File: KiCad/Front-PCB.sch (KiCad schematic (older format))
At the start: 0 parts

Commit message: front PCB schematic complete
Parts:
- added J1: CONN_01X20, symbol CONN_01X20
- added R19: R, symbol R
- added S1-Left, S2-Up, S3-Right, S4-Down: RP3502, symbol RP3502
- added S5-Start, S6-Stop: RP3508, symbol RP3508
- added S7-Door-Contact: A0151B, symbol A0151B
- added U?: MAX7219, symbol MAX7219
- added U?: LTC-4727JR, symbol LTC-4727JR
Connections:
- net labels added: +5V, GND
- wire segments 0 -> 96
- no-connect marks 0 -> 4

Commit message: front panel erc
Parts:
- removed U?: MAX7219, symbol MAX7219
- removed U?: LTC-4727JR, symbol LTC-4727JR
- added R1, R2, R3, R4, R5, R6: 1k, symbol R
- added R20, R21: 500, symbol R
- added U1: MAX7219, symbol MAX7219
- added U2: LTC-4727JR, symbol LTC-4727JR
- J1: value CONN_01X20 -> HLW20R-2C7LF
- R19: value R -> 10k
- S1: renamed from S1-Left; symbol RP3502 -> RP3502-RESCUE-Front-PCB
- S2: renamed from S2-Up; symbol RP3502 -> RP3502-RESCUE-Front-PCB
- S3: renamed from S3-Right; symbol RP3502 -> RP3502-RESCUE-Front-PCB
- S4: renamed from S4-Down; symbol RP3502 -> RP3502-RESCUE-Front-PCB
- S5: renamed from S5-Start; symbol RP3508 -> RP3508-RESCUE-Front-PCB
- S6: renamed from S6-Stop; symbol RP3508 -> RP3508-RESCUE-Front-PCB
- renumbered S7-Door-Contact to S7
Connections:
- wire segments 96 -> 109
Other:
- moved on the sheet: S3

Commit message: kicad footprints and unrouted layout
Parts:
- added P1: Mounting Vias, Easy-PCB-footprints:10-32, symbol CONN_01X01
- added P2, P3, P4: CONN_01X01, Easy-PCB-footprints:10-32, symbol CONN_01X01
- J1: footprint (none) -> Easy-PCB-Footprints:HLW20R-2C7LF
- R1, R19, R2, R20, R21, R3, R4, R5, R6: footprint (none) -> Discret:R4
- S1, S2, S3, S4: footprint (none) -> Easy-PCB-Footprints:RP3502
- S5, S6: footprint (none) -> Easy-PCB-Footprints:RP3508; symbol RP3508-RESCUE-Front-PCB -> RP3508
- S7: footprint (none) -> Easy-PCB-Footprints:A0151B
- U1: footprint (none) -> Easy-PCB-footprints:4824-3000-CP
- U2: footprint (none) -> Easy-PCB-footprints:LTC-4727JR
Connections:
- wire segments 109 -> 115
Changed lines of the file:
@@
 F 0 "R19" V 9230 1800 50  0000 C CNN
 F 1 "10k" V 9150 1800 50  0000 C CNN
-F 2 "" V 9080 1800 30  0000 C CNN
+F 2 "Discret:R4" V 9080 1800 30  0001 C CNN
 F 3 "" H 9150 1800 30  0000 C CNN
 	1    9150 1800
@@
 F 0 "S1" H 1300 6400 60  0000 C CNN
 F 1 "RP3502" H 1300 5900 60  0000 C CNN
-F 2 "" H 1300 6050 60  0000 C CNN
+F 2 "Easy-PCB-Footprints:RP3502" H 1300 6050 60  0001 C CNN
 F 3 "" H 1300 6050 60  0000 C CNN
 	1    1300 6050
@@
 F 0 "S4" H 2300 6800 60  0000 C CNN
 F 1 "RP3502" H 2300 6300 60  0000 C CNN
-F 2 "" H 2300 6450 60  0000 C CNN
+F 2 "Easy-PCB-Footprints:RP3502" H 2300 6450 60  0001 C CNN
 F 3 "" H 2300 6450 60  0000 C CNN
 	1    2300 6450
@@
 F 0 "S2" H 2400 6050 60  0000 C CNN
 F 1 "RP3502" H 2400 5550 60  0000 C CNN
-F 2 "" H 2400 5700 60  0000 C CNN
+F 2 "Easy-PCB-Footprints:RP3502" H 2400 5700 60  0001 C CNN
 F 3 "" H 2400 5700 60  0000 C CNN
 	1    2400 5700
@@
 F 0 "S3" H 3500 6350 60  0000 C CNN
 F 1 "RP3502" H 3500 5850 60  0000 C CNN
-F 2 "" H 3500 6000 60  0000 C CNN
+F 2 "Easy-PCB-Footprints:RP3502" H 3500 6000 60  0001 C CNN
 F 3 "" H 3500 6000 60  0000 C CNN
 	1    3500 6000
@@
 $EndComp
 $Comp
-L RP3508-RESCUE-Front-PCB S5
+L RP3508 S5
 U 1 1 5652B631
 P 4500 6000
 F 0 "S5" H 4500 6500 60  0000 C CNN
 F 1 "RP3508" H 4500 6400 60  0000 C CNN
-F 2 "" H 4500 6000 60  0000 C CNN
+F 2 "Easy-PCB-Footprints:RP3508" H 4500 6000 60  0001 C CNN
 F 3 "" H 4500 6000 60  0000 C CNN
 	1    4500 6000
@@
 $EndComp
 $Comp
-L RP3508-RESCUE-Front-PCB S6
+L RP3508 S6
 U 1 1 5652B70B
 P 5800 6200
 F 0 "S6" H 5800 6700 60  0000 C CNN
 F 1 "RP3508" H 5800 6600 60  0000 C CNN
-F 2 "" H 5800 6200 60  0000 C CNN
+F 2 "Easy-PCB-Footprints:RP3508" H 5800 6200 60  0001 C CNN
 F 3 "" H 5800 6200 60  0000 C CNN
 	1    5800 6200
@@
 F 0 "S7" H 3900 7850 60  0000 C CNN
 F 1 "A0151B" H 3900 6800 60  0000 C CNN
-F 2 "" H 3900 7250 60  0000 C CNN
+F 2 "Easy-PCB-Footprints:A0151B" H 3900 7250 60  0001 C CNN
 F 3 "" H 3900 7250 60  0000 C CNN
 	1    3900 7250
@@
 F 0 "R1" V 1780 6350 50  0000 C CNN
 F 1 "1k" V 1700 6350 50  0000 C CNN
-F 2 "" V 1630 6350 30  0000 C CNN
+F 2 "Discret:R4" V 1630 6350 30  0001 C CNN
 F 3 "" H 1700 6350 30  0000 C CNN
 	1    1700 6350
@@
 F 0 "R2" V 2880 5950 50  0000 C CNN
 F 1 "1k" V 2800 5950 50  0000 C CNN
-F 2 "" V 2730 5950 30  0000 C CNN
+F 2 "Discret:R4" V 2730 5950 30  0001 C CNN
 F 3 "" H 2800 5950 30  0000 C CNN
 	1    2800 5950
@@
 F 0 "R4" V 2880 6700 50  0000 C CNN
 F 1 "1k" V 2800 6700 50  0000 C CNN
-F 2 "" V 2730 6700 30  0000 C CNN
+F 2 "Discret:R4" V 2730 6700 30  0001 C CNN
 F 3 "" H 2800 6700 30  0000 C CNN
 	1    2800 6700
@@
 F 0 "R3" V 4130 6150 50  0000 C CNN
 F 1 "1k" V 4050 6150 50  0000 C CNN
-F 2 "" V 3980 6150 30  0000 C CNN
+F 2 "Discret:R4" V 3980 6150 30  0001 C CNN
 F 3 "" H 4050 6150 30  0000 C CNN
 	1    4050 6150
@@
 F 0 "R5" V 5080 6150 50  0000 C CNN
 F 1 "1k" V 5000 6150 50  0000 C CNN
-F 2 "" V 4930 6150 30  0000 C CNN
+F 2 "Discret:R4" V 4930 6150 30  0001 C CNN
 F 3 "" H 5000 6150 30  0000 C CNN
 	1    5000 6150
@@
 F 0 "R20" V 5280 6050 50  0000 C CNN
 F 1 "500" V 5200 6050 50  0000 C CNN
-F 2 "" V 5130 6050 30  0000 C CNN
+F 2 "Discret:R4" V 5130 6050 30  0001 C CNN
 F 3 "" H 5200 6050 30  0000 C CNN
 	1    5200 6050
@@
 F 0 "R6" V 6480 6200 50  0000 C CNN
 F 1 "1k" V 6400 6200 50  0000 C CNN
-F 2 "" V 6330 6200 30  0000 C CNN
+F 2 "Discret:R4" V 6330 6200 30  0001 C CNN
 F 3 "" H 6400 6200 30  0000 C CNN
 	1    6400 6200
@@
 F 0 "R21" V 6780 6000 50  0000 C CNN
 F 1 "500" V 6700 6000 50  0000 C CNN
-F 2 "" V 6630 6000 30  0000 C CNN
+F 2 "Discret:R4" V 6630 6000 30  0001 C CNN
 F 3 "" H 6700 6000 30  0000 C CNN
 	1    6700 6000
@@
 F 0 "J1" H 9900 6250 50  0000 C CNN
 F 1 "HLW20R-2C7LF" V 10050 5150 50  0000 C CNN
-F 2 "" H 9900 5150 60  0000 C CNN
+F 2 "Easy-PCB-Footprints:HLW20R-2C7LF" H 9900 5150 60  0001 C CNN
 F 3 "" H 9900 5150 60  0000 C CNN
 	1    9900 5150
@@
 F 0 "U2" H 4000 550 100 0000 L CNN
 F 1 "LTC-4727JR" H 3050 550 100 0000 C CNN
-F 2 "" H 3600 1850 60  0000 C CNN
+F 2 "Easy-PCB-footprints:LTC-4727JR" H 3600 1850 60  0001 C CNN
 F 3 "" H 3600 1850 60  0000 C CNN
 	1    3600 1850
@@
 F 0 "U1" H 8250 3350 60  0000 L CNN
 F 1 "MAX7219" H 8450 3450 60  0000 C CNN
-F 2 "" H 8300 2950 60  0000 C CNN
+F 2 "Easy-PCB-footprints:4824-3000-CP" H 8300 2950 60  0001 C CNN
 F 3 "" H 8300 2950 60  0000 C CNN
 	1    8300 2950
 	1    0    0    -1
 $EndComp
+$Comp
+L CONN_01X01 P1
+U 1 1 5655FFD6
+P 900 7000
+F 0 "P1" H 900 7100 50  0000 C CNN
+F 1 "Mounting Vias" V 1100 6650 50  0000 C CNN
+F 2 "Easy-PCB-footprints:10-32" H 900 7000 60  0001 C CNN
+F 3 "" H 900 7000 60  0000 C CNN
+	1    900  7000
+	-1   0    0    -1
+$EndComp
+$Comp
+L CONN_01X01 P2
+U 1 1 565600BD
+P 900 7250
+F 0 "P2" H 900 7350 50  0000 C CNN
+F 1 "CONN_01X01" V 1000 7250 50  0001 C CNN
+F 2 "Easy-PCB-footprints:10-32" H 900 7250 60  0001 C CNN
+F 3 "" H 900 7250 60  0000 C CNN
+	1    900  7250
+	-1   0    0    -1
+$EndComp
+$Comp
+L CONN_01X01 P3
+U 1 1 5656018C
+P 900 7500
+F 0 "P3" H 900 7600 50  0000 C CNN
+F 1 "CONN_01X01" V 1000 7500 50  0001 C CNN
+F 2 "Easy-PCB-footprints:10-32" H 900 7500 60  0001 C CNN
+F 3 "" H 900 7500 60  0000 C CNN
+	1    900  7500
+	-1   0    0    -1
+$EndComp
+$Comp
+L CONN_01X01 P4
+U 1 1 565601F5
+P 900 7750
+F 0 "P4" H 900 7850 50  0000 C CNN
+F 1 "CONN_01X01" V 1000 7750 50  0001 C CNN
+F 2 "Easy-PCB-footprints:10-32" H 900 7750 60  0001 C CNN
+F 3 "" H 900 7750 60  0000 C CNN
+	1    900  7750
+	-1   0    0    -1
+$EndComp
+$Comp
+L GND #PWR015
+U 1 1 56560FC4
+P 1400 7350
+F 0 "#PWR015" H 1400 7100 50  0001 C CNN
+F 1 "GND" H 1400 7200 50  0000 C CNN
+F 2 "" H 1400 7350 60  0000 C CNN
+F 3 "" H 1400 7350 60  0000 C CNN
+	1    1400 7350
+	1    0    0    -1
+$EndComp
+Wire Wire Line
+	1400 7350 1400 7250
+Wire Wire Line
+	1400 7250 1100 7250
+Wire Wire Line
+	1100 7000 1250 7000
+Wire Wire Line
+	1250 7000 1250 7750
+Connection ~ 1250 7250
+Wire Wire Line
+	1250 7500 1100 7500
+Wire Wire Line
+	1250 7750 1100 7750
+Connection ~ 1250 7500
 $EndSCHEMATC

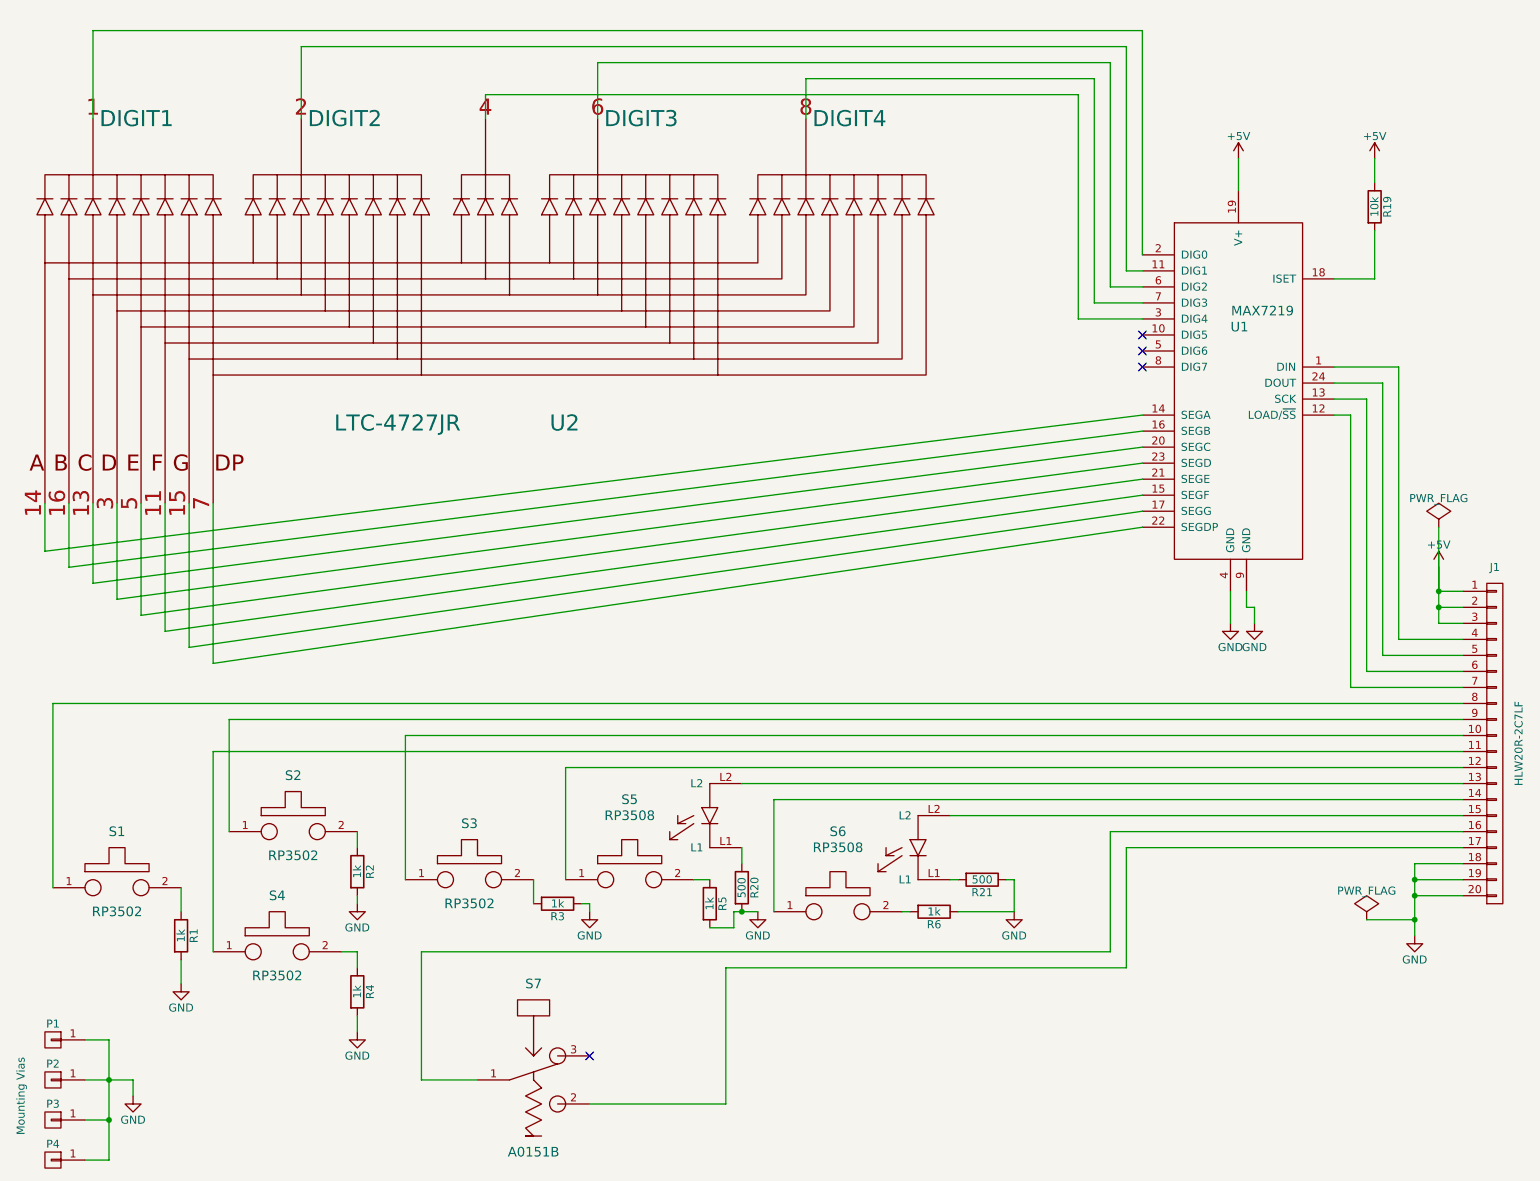
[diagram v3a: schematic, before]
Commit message: front panel pcb routing complete
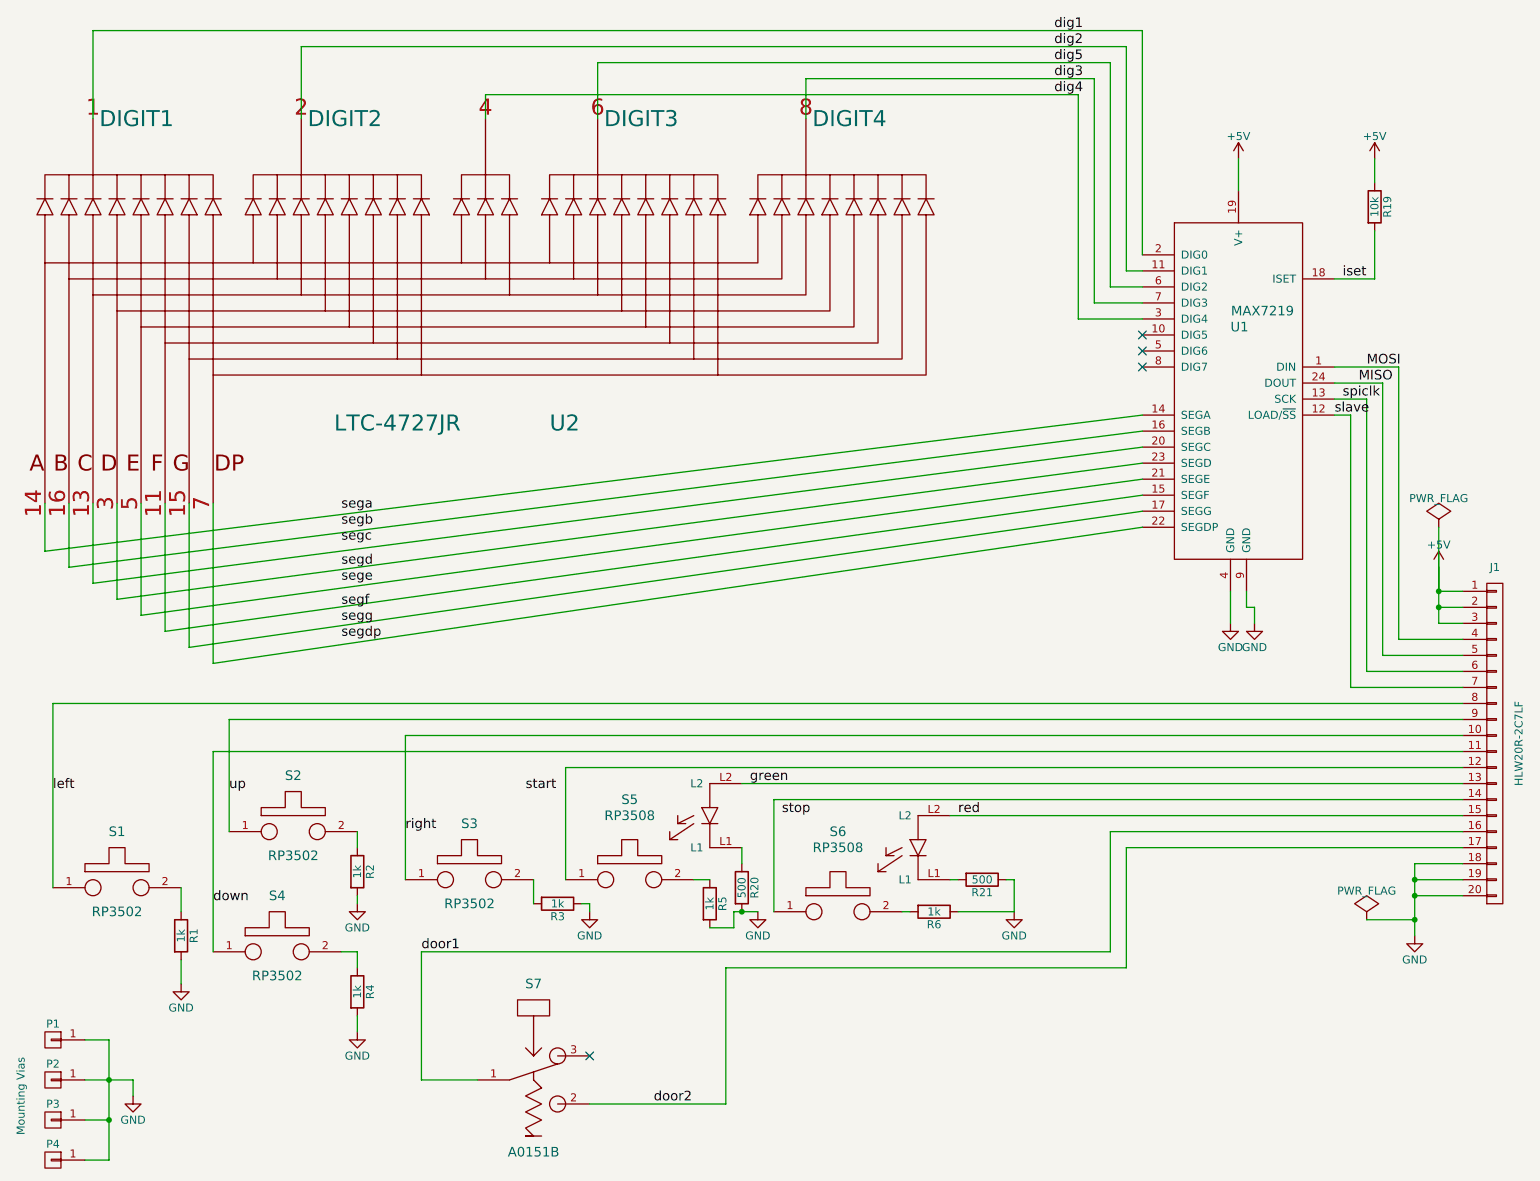
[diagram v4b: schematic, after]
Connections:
- net iset: now reaches R19.2, U1.18 (ISET)
- net left: now reaches J1.8 (P8), S1.1
- net down: now reaches J1.11 (P11), S4.1
- net up: now reaches J1.9 (P9), S2.1
- net right: now reaches J1.10 (P10), S3.1
- net green: now reaches J1.13 (P13), S5.L2
- net red: now reaches J1.15 (P15), S6.L2
- net door1: now reaches J1.16 (P16), S7.1
- net door2: now reaches J1.17 (P17), S7.2
- net MOSI: now reaches J1.4 (P4), U1.1 (DIN)
- net MISO: now reaches J1.5 (P5), U1.24 (DOUT)
- net spiclk: now reaches J1.6 (P6), U1.13 (SCK)
- net slave: now reaches J1.7 (P7), U1.12 (LOAD/~SS)
- net dig1: now reaches U1.2 (DIG0), U2.1 (DIGIT1)
- net dig2: now reaches U1.11 (DIG1), U2.2 (DIGIT2)
- net dig4: now reaches U1.3 (DIG4), U2.4
- net dig5: now reaches U1.6 (DIG2), U2.6 (DIGIT3)
- net dig3: now reaches U1.7 (DIG3), U2.8 (DIGIT4)
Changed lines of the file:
@@
 	1250 7750 1100 7750
 Connection ~ 1250 7500
+Text Label 7150 700  0    60   ~ 0
+dig1
+Text Label 7150 800  0    60   ~ 0
+dig2
+Text Label 7150 900  0    60   ~ 0
+dig5
+Text Label 7150 1000 0    60   ~ 0
+dig3
+Text Label 7150 1100 0    60   ~ 0
+dig4
+Text Label 8950 2250 0    60   ~ 0
+iset
+Text Label 9100 2800 0    60   ~ 0
+MOSI
+Text Label 9050 2900 0    60   ~ 0
+MISO
+Text Label 8950 3000 0    60   ~ 0
+spiclk
+Text Label 8900 3100 0    60   ~ 0
+slave
+Text Label 2700 3700 0    60   ~ 0
+sega
+Text Label 2700 3800 0    60   ~ 0
+segb
+Text Label 2700 3900 0    60   ~ 0
+segc
+Text Label 2700 4050 0    60   ~ 0
+segd
+Text Label 2700 4150 0    60   ~ 0
+sege
+Text Label 2700 4300 0    60   ~ 0
+segf
+Text Label 2700 4400 0    60   ~ 0
+segg
+Text Label 2700 4500 0    60   ~ 0
+segdp
+Text Label 900  5450 0    60   ~ 0
+left
+Text Label 2000 5450 0    60   ~ 0
+up
+Text Label 1900 6150 0    60   ~ 0
+down
+Text Label 3100 5700 0    60   ~ 0
+right
+Text Label 3850 5450 0    60   ~ 0
+start
+Text Label 5450 5600 0    60   ~ 0
+stop
+Text Label 5250 5400 0    60   ~ 0
+green
+Text Label 6550 5600 0    60   ~ 0
+red
+Text Label 3200 6450 0    60   ~ 0
+door1
+Text Label 4650 7400 0    60   ~ 0
+door2
 $EndSCHEMATC
